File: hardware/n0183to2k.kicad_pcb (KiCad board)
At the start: 2 copper layers, 60 x 60 mm, 41 parts, among them J1 NMEA0183 (wind), J2 Conn_01x06_Male, J3 Conn_01x05_Male, J4 RJ45, J5 RJ45, J6 Conn_02x03_Odd_Even, Q1 BSS123, Q2 DMG2307L, Q3 BSS123, U1 PIC18F27Q84_ISS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

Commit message: properly place the BME280 module connector, and start wriing it.
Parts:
- moved J2 11.5 mm to (105.2, 106.3), turned to 180 degrees
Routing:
- net +3V3: track 96.9 -> 106.7 mm
- net /SCL: track 3.17 -> 12.4 mm
- net /SDA: track 3.17 -> 10.8 mm
- net Net-(D4-Pad1): track 89.8 -> 91.8 mm
- net /12V_ON: track 105.3 -> 106.1 mm

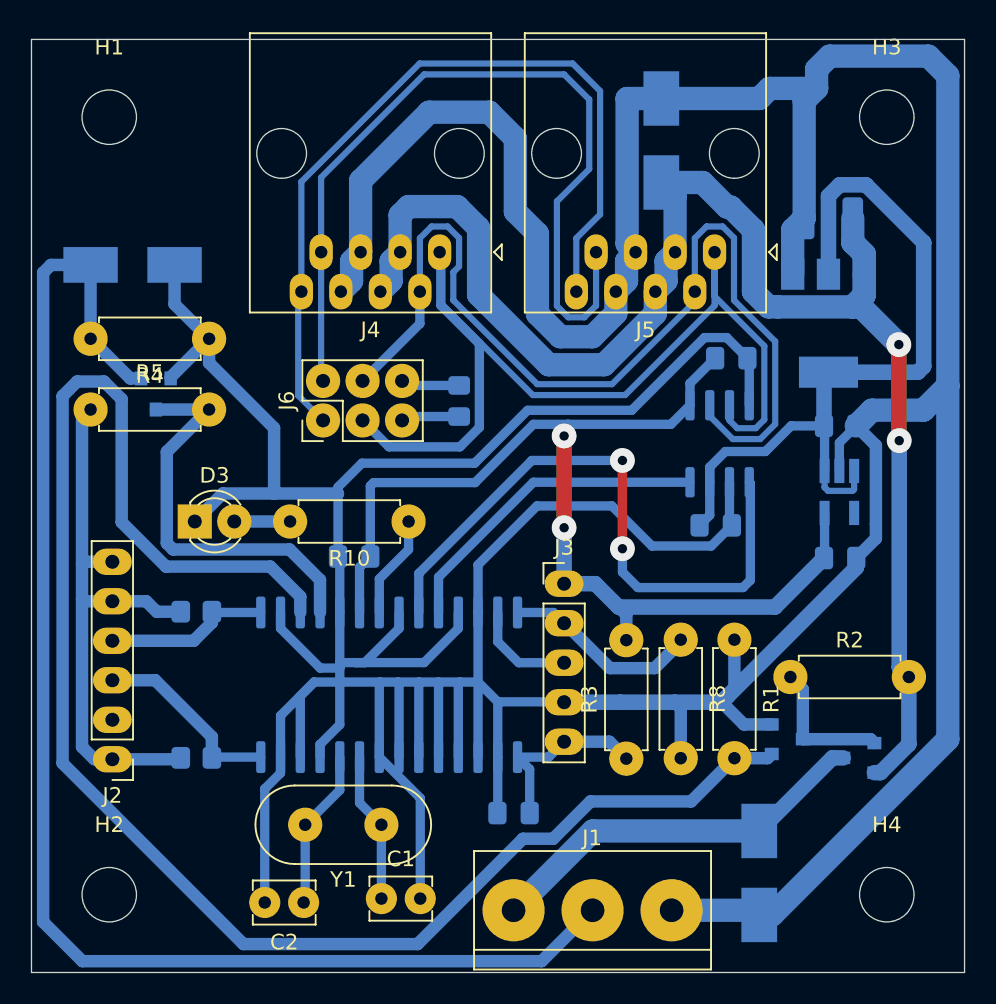
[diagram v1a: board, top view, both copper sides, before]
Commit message: move 12V_ON to RA2, closer to the mosfet.
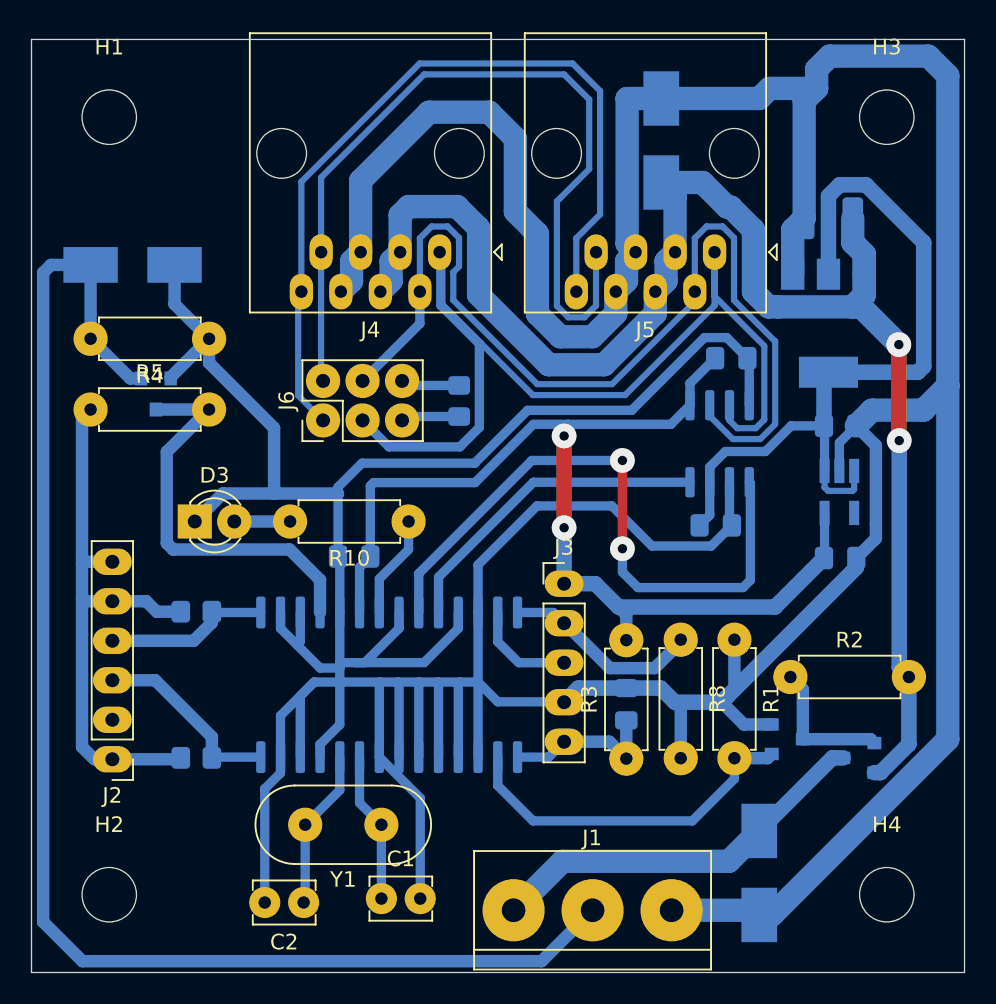
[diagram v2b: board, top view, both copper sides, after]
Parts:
- moved C7 10.1 mm to (138.2, 102.8), turned to 270 degrees
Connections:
- U1 pad 17: /12V_ON -> GND
- U1 pad 2: GND -> /12V_ON
- U3 pad 4: (no net) -> Net-(U3-Pad4)
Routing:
- net /12V_ON: track 106.1 -> 22.9 mm
- net GND: track 425.1 -> 420.9 mm
- net /MCLR: track 11.8 -> 10.3 mm
